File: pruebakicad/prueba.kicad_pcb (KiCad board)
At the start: 2 copper layers, 33 parts, among them J1 Conn_01x08_RC522, J2 Conn_01x04_MountingPin, J3 Conn_01x03, J4 Conn_2Rows-15Pins, J5 Conn_01x04, Q1 BSS138, Q2 BSS138, U1 TLV1117-33, U2 TLV1117-50, U3 ESP32-WROOM-32

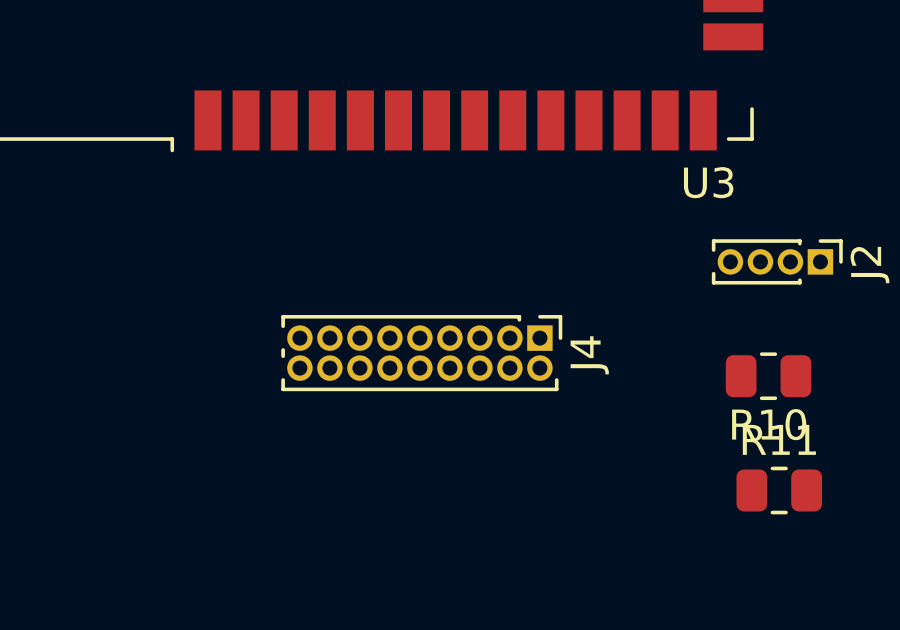
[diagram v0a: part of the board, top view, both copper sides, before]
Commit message: wires updated
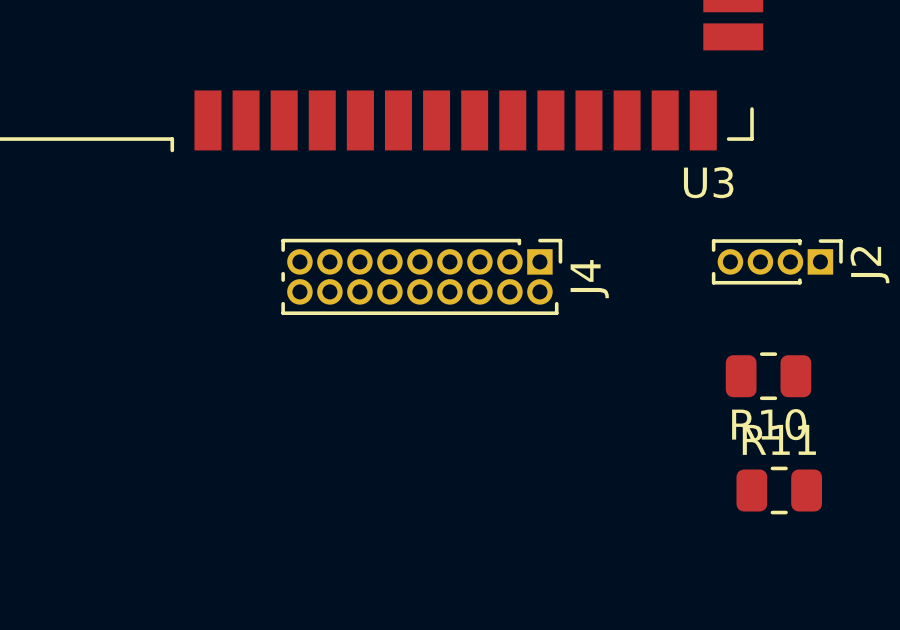
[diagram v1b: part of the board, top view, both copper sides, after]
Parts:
- moved J4 2.54 mm to (53.3, 114.3)
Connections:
- J4 pad 12: /sensVP -> Net-(J4-Pad12)
- J4 pad 13: /IO26 -> /sensVN
- J4 pad 14: /sensVN -> /sensVP
- J4 pad 15: GND -> +3V3
- J4 pad 16: +5V -> GND

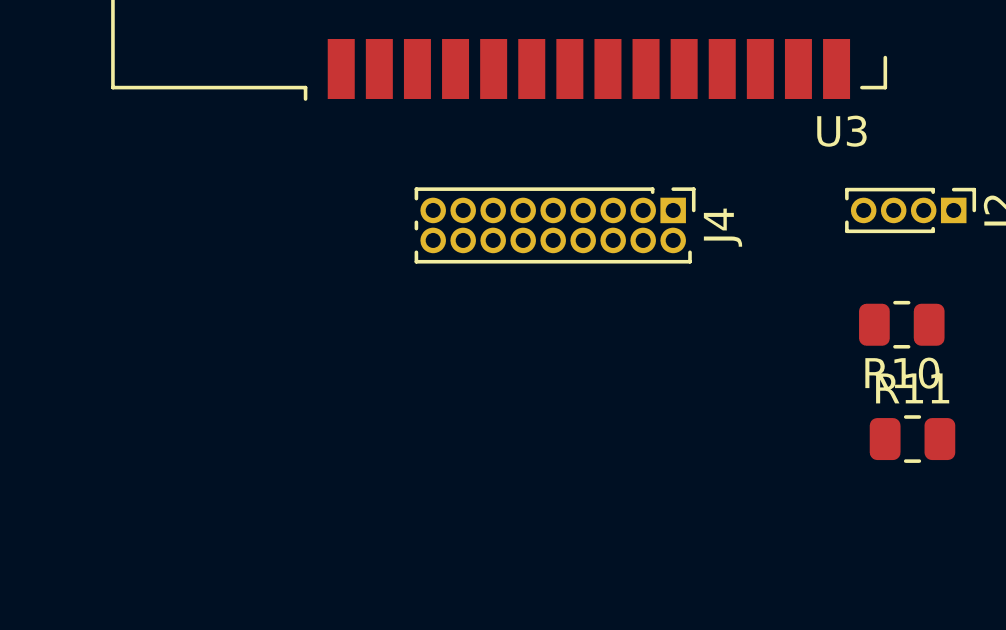
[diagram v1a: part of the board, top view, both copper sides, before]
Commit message: wires updated
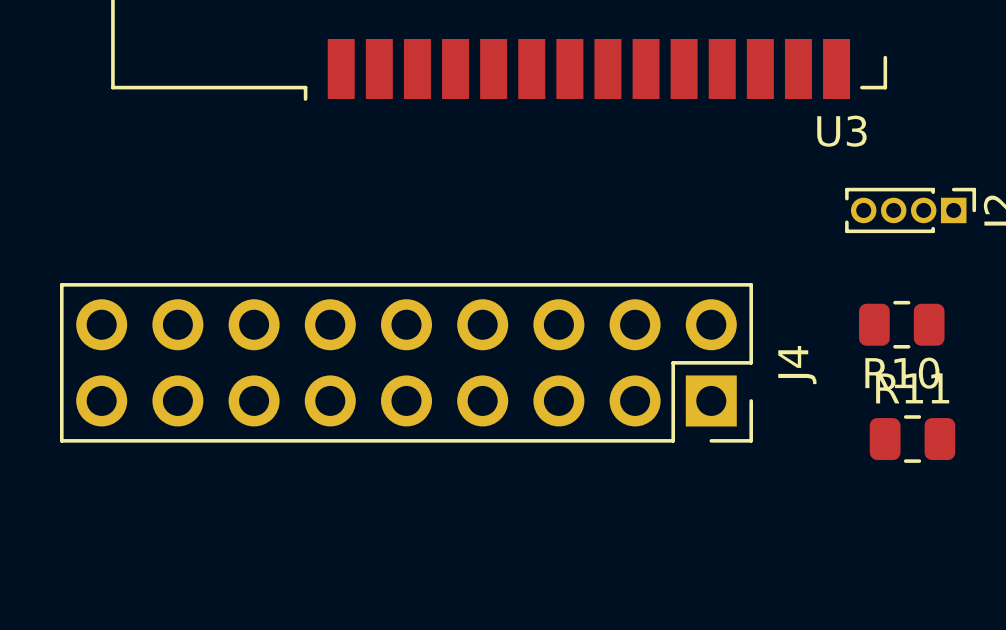
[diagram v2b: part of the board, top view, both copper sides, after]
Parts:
- J4: footprint Connector_PinHeader_1.00mm:PinHeader_2x09_P1.00mm_Vertical -> Connector_PinSocket_2.54mm:PinSocket_2x09_P2.54mm_Vertical
- moved J4 6.48 mm to (54.6, 120.7)
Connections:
- J4 pad 10: /IO35 -> /IO32
- J4 pad 11: /IO25 -> /IO35
- J4 pad 12: Net-(J4-Pad12) -> /IO34
- J4 pad 2: /IO27 -> Net-(J4-Pad2)
- J4 pad 3: /IO13 -> Net-(J4-Pad3)
- J4 pad 4: /IO32 -> Net-(J4-Pad4)
- J4 pad 5: /IO15 -> Net-(J4-Pad5)
- J4 pad 6: /IO33 -> /IO27
- J4 pad 7: /IO16 -> /IO26
- J4 pad 8: /IO34 -> /IO25
- J4 pad 9: /IO17 -> /IO33
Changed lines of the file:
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@@
     (zones 0)
     (modules 33)
-    (nets 49)
+    (nets 52)
   )
   (page A4)
@@
   (net 46 /esp32-wroom/IO0)
   (net 47 "Net-(U3-Pad32)")
-  (net 48 "Net-(J4-Pad12)")
+  (net 48 "Net-(J4-Pad4)")
+  (net 49 "Net-(J4-Pad2)")
+  (net 50 "Net-(J4-Pad5)")
+  (net 51 "Net-(J4-Pad3)")
   (net_class Default "This is the default net class."
     (clearance 0.2)
@@
     (add_net "Net-(C5-Pad1)")
     (add_net "Net-(J1-Pad5)")
-    (add_net "Net-(J4-Pad12)")
+    (add_net "Net-(J4-Pad2)")
+    (add_net "Net-(J4-Pad3)")
+    (add_net "Net-(J4-Pad4)")
+    (add_net "Net-(J4-Pad5)")
     (add_net "Net-(LedRed1-Pad2)")
     (add_net "Net-(Q1-Pad1)")
@@
     (add_net "Net-(U3-Pad22)")
     (add_net "Net-(U3-Pad32)")
+  )
+  (module Connector_PinSocket_2.54mm:PinSocket_2x09_P2.54mm_Vertical (layer F.Cu)
+    (at 54.61 120.65 270)
+    (descr "Through hole straight socket strip, 2x09, 2.54mm pitch, double cols (from Kicad 4.0.7), script generated")
+    (tags "Through hole socket strip THT 2x09 2.54mm double row")
+    (fp_text reference J4 (at -1.27 -2.77 90) (layer F.SilkS)
+      (effects (font (size 1 1) (thickness 0.15)))
+    )
+    (fp_text value Conn_2Rows-15Pins (at -1.27 23.09 90) (layer F.Fab)
+      (effects (font (size 1 1) (thickness 0.15)))
+    )
+    (fp_text user %R (at -1.27 10.16) (layer F.Fab)
+      (effects (font (size 1 1) (thickness 0.15)))
+    )
+    (fp_line (start -3.81 -1.27) (end 0.27 -1.27) (layer F.Fab) (width 0.1))
+    (fp_line (start 0.27 -1.27) (end 1.27 -0.27) (layer F.Fab) (width 0.1))
+    (fp_line (start 1.27 -0.27) (end 1.27 21.59) (layer F.Fab) (width 0.1))
+    (fp_line (start 1.27 21.59) (end -3.81 21.59) (layer F.Fab) (width 0.1))
+    (fp_line (start -3.81 21.59) (end -3.81 -1.27) (layer F.Fab) (width 0.1))
+    (fp_line (start -3.87 -1.33) (end -1.27 -1.33) (layer F.SilkS) (width 0.12))
+    (fp_line (start -3.87 -1.33) (end -3.87 21.65) (layer F.SilkS) (width 0.12))
+    (fp_line (start -3.87 21.65) (end 1.33 21.65) (layer F.SilkS) (width 0.12))
+    (fp_line (start 1.33 1.27) (end 1.33 21.65) (layer F.SilkS) (width 0.12))
+    (fp_line (start -1.27 1.27) (end 1.33 1.27) (layer F.SilkS) (width 0.12))
+    (fp_line (start -1.27 -1.33) (end -1.27 1.27) (layer F.SilkS) (width 0.12))
+    (fp_line (start 1.33 -1.33) (end 1.33 0) (layer F.SilkS) (width 0.12))
+    (fp_line (start 0 -1.33) (end 1.33 -1.33) (layer F.SilkS) (width 0.12))
+    (fp_line (start -4.34 -1.8) (end 1.76 -1.8) (layer F.CrtYd) (width 0.05))
+    (fp_line (start 1.76 -1.8) (end 1.76 22.1) (layer F.CrtYd) (width 0.05))
+    (fp_line (start 1.76 22.1) (end -4.34 22.1) (layer F.CrtYd) (width 0.05))
+    (fp_line (start -4.34 22.1) (end -4.34 -1.8) (layer F.CrtYd) (width 0.05))
+    (pad 18 thru_hole oval (at -2.54 20.32 270) (size 1.7 1.7) (drill 1) (layers *.Cu *.Mask))
+    (pad 17 thru_hole oval (at 0 20.32 270) (size 1.7 1.7) (drill 1) (layers *.Cu *.Mask)
+      (net 4 GND))
+    (pad 16 thru_hole oval (at -2.54 17.78 270) (size 1.7 1.7) (drill 1) (layers *.Cu *.Mask)
+      (net 4 GND))
+    (pad 15 thru_hole oval (at 0 17.78 270) (size 1.7 1.7) (drill 1) (layers *.Cu *.Mask)
+      (net 5 +3V3))
+    (pad 14 thru_hole oval (at -2.54 15.24 270) (size 1.7 1.7) (drill 1) (layers *.Cu *.Mask)
+      (net 29 /sensVP))
+    (pad 13 thru_hole oval (at 0 15.24 270) (size 1.7 1.7) (drill 1) (layers *.Cu *.Mask)
+      (net 31 /sensVN))
+    (pad 12 thru_hole oval (at -2.54 12.7 270) (size 1.7 1.7) (drill 1) (layers *.Cu *.Mask)
+      (net 25 /IO34))
+    (pad 11 thru_hole oval (at 0 12.7 270) (size 1.7 1.7) (drill 1) (layers *.Cu *.Mask)
+      (net 27 /IO35))
+    (pad 10 thru_hole oval (at -2.54 10.16 270) (size 1.7 1.7) (drill 1) (layers *.Cu *.Mask)
+      (net 21 /IO32))
+    (pad 9 thru_hole oval (at 0 10.16 270) (size 1.7 1.7) (drill 1) (layers *.Cu *.Mask)
+      (net 23 /IO33))
+    (pad 8 thru_hole oval (at -2.54 7.62 270) (size 1.7 1.7) (drill 1) (layers *.Cu *.Mask)
+      (net 28 /IO25))
+    (pad 7 thru_hole oval (at 0 7.62 270) (size 1.7 1.7) (drill 1) (layers *.Cu *.Mask)
+      (net 30 /IO26))
+    (pad 6 thru_hole oval (at -2.54 5.08 270) (size 1.7 1.7) (drill 1) (layers *.Cu *.Mask)
+      (net 20 /IO27))
+    (pad 5 thru_hole oval (at 0 5.08 270) (size 1.7 1.7) (drill 1) (layers *.Cu *.Mask)
+      (net 50 "Net-(J4-Pad5)"))
+    (pad 4 thru_hole oval (at -2.54 2.54 270) (size 1.7 1.7) (drill 1) (layers *.Cu *.Mask)
+      (net 48 "Net-(J4-Pad4)"))
+    (pad 3 thru_hole oval (at 0 2.54 270) (size 1.7 1.7) (drill 1) (layers *.Cu *.Mask)
+      (net 51 "Net-(J4-Pad3)"))
+    (pad 2 thru_hole oval (at -2.54 0 270) (size 1.7 1.7) (drill 1) (layers *.Cu *.Mask)
+      (net 49 "Net-(J4-Pad2)"))
+    (pad 1 thru_hole rect (at 0 0 270) (size 1.7 1.7) (drill 1) (layers *.Cu *.Mask)
+      (net 5 +3V3))
+    (model ${KISYS3DMOD}/Connector_PinSocket_2.54mm.3dshapes/PinSocket_2x09_P2.54mm_Vertical.wrl
+      (at (xyz 0 0 0))
+      (scale (xyz 1 1 1))
+      (rotate (xyz 0 0 0))
+    )
   )
   (module LED_SMD:LED_0805_2012Metric (layer F.Cu)
@@
       (at (xyz 0 0 0))
       (scale (xyz 1 1 1))
-      (rotate (xyz 0 0 0))
-    )
-  )
-  (module Connector_PinHeader_1.00mm:PinHeader_2x09_P1.00mm_Vertical (layer F.Cu)
-    (at 53.34 114.3 270)
-    (descr "Through hole straight pin header, 2x09, 1.00mm pitch, double rows")
-    (tags "Through hole pin header THT 2x09 1.00mm double row")
-    (fp_text reference J4 (at 0.5 -1.56 90) (layer F.SilkS)
-      (effects (font (size 1 1) (thickness 0.15)))
-    )
-    (fp_text value Conn_2Rows-15Pins (at 0.5 9.56 90) (layer F.Fab)
-      (effects (font (size 1 1) (thickness 0.15)))
-    )
-    (fp_line (start -0.075 -0.5) (end 1.65 -0.5) (layer F.Fab) (width 0.1))
-    (fp_line (start 1.65 -0.5) (end 1.65 8.5) (layer F.Fab) (width 0.1))
-    (fp_line (start 1.65 8.5) (end -0.65 8.5) (layer F.Fab) (width 0.1))
-    (fp_line (start -0.65 8.5) (end -0.65 0.075) (layer F.Fab) (width 0.1))
-    (fp_line (start -0.65 0.075) (end -0.075 -0.5) (layer F.Fab) (width 0.1))
-    (fp_line (start -0.71 8.56) (end -0.394493 8.56) (layer F.SilkS) (width 0.12))
-    (fp_line (start 1.394493 8.56) (end 1.71 8.56) (layer F.SilkS) (width 0.12))
-    (fp_line (start 0.394493 8.56) (end 0.605507 8.56) (layer F.SilkS) (width 0.12))
-    (fp_line (start -0.71 0.685) (end -0.71 8.56) (layer F.SilkS) (width 0.12))
-    (fp_line (start 1.71 -0.56) (end 1.71 8.56) (layer F.SilkS) (width 0.12))
-    (fp_line (start -0.71 0.685) (end -0.608276 0.685) (layer F.SilkS) (width 0.12))
-    (fp_line (start 1.394493 -0.56) (end 1.71 -0.56) (layer F.SilkS) (width 0.12))
-    (fp_line (start -0.71 0) (end -0.71 -0.685) (layer F.SilkS) (width 0.12))
-    (fp_line (start -0.71 -0.685) (end 0 -0.685) (layer F.SilkS) (width 0.12))
-    (fp_line (start -1.15 -1) (end -1.15 9) (layer F.CrtYd) (width 0.05))
-    (fp_line (start -1.15 9) (end 2.15 9) (layer F.CrtYd) (width 0.05))
-    (fp_line (start 2.15 9) (end 2.15 -1) (layer F.CrtYd) (width 0.05))
-    (fp_line (start 2.15 -1) (end -1.15 -1) (layer F.CrtYd) (width 0.05))
-    (fp_text user %R (at 0.5 4) (layer F.Fab)
-      (effects (font (size 1 1) (thickness 0.15)))
-    )
-    (pad 1 thru_hole rect (at 0 0 270) (size 0.85 0.85) (drill 0.5) (layers *.Cu *.Mask)
-      (net 5 +3V3))
-    (pad 2 thru_hole oval (at 1 0 270) (size 0.85 0.85) (drill 0.5) (layers *.Cu *.Mask)
-      (net 20 /IO27))
-    (pad 3 thru_hole oval (at 0 1 270) (size 0.85 0.85) (drill 0.5) (layers *.Cu *.Mask)
-      (net 2 /IO13))
-    (pad 4 thru_hole oval (at 1 1 270) (size 0.85 0.85) (drill 0.5) (layers *.Cu *.Mask)
-      (net 21 /IO32))
-    (pad 5 thru_hole oval (at 0 2 270) (size 0.85 0.85) (drill 0.5) (layers *.Cu *.Mask)
-      (net 22 /IO15))
-    (pad 6 thru_hole oval (at 1 2 270) (size 0.85 0.85) (drill 0.5) (layers *.Cu *.Mask)
-      (net 23 /IO33))
-    (pad 7 thru_hole oval (at 0 3 270) (size 0.85 0.85) (drill 0.5) (layers *.Cu *.Mask)
-      (net 24 /IO16))
-    (pad 8 thru_hole oval (at 1 3 270) (size 0.85 0.85) (drill 0.5) (layers *.Cu *.Mask)
-      (net 25 /IO34))
-    (pad 9 thru_hole oval (at 0 4 270) (size 0.85 0.85) (drill 0.5) (layers *.Cu *.Mask)
-      (net 26 /IO17))
-    (pad 10 thru_hole oval (at 1 4 270) (size 0.85 0.85) (drill 0.5) (layers *.Cu *.Mask)
-      (net 27 /IO35))
-    (pad 11 thru_hole oval (at 0 5 270) (size 0.85 0.85) (drill 0.5) (layers *.Cu *.Mask)
-      (net 28 /IO25))
-    (pad 12 thru_hole oval (at 1 5 270) (size 0.85 0.85) (drill 0.5) (layers *.Cu *.Mask)
-      (net 48 "Net-(J4-Pad12)"))
-    (pad 13 thru_hole oval (at 0 6 270) (size 0.85 0.85) (drill 0.5) (layers *.Cu *.Mask)
-      (net 31 /sensVN))
-    (pad 14 thru_hole oval (at 1 6 270) (size 0.85 0.85) (drill 0.5) (layers *.Cu *.Mask)
-      (net 29 /sensVP))
-    (pad 15 thru_hole oval (at 0 7 270) (size 0.85 0.85) (drill 0.5) (layers *.Cu *.Mask)
-      (net 5 +3V3))
-    (pad 16 thru_hole oval (at 1 7 270) (size 0.85 0.85) (drill 0.5) (layers *.Cu *.Mask)
-      (net 4 GND))
-    (pad 17 thru_hole oval (at 0 8 270) (size 0.85 0.85) (drill 0.5) (layers *.Cu *.Mask)
-      (net 4 GND))
-    (pad 18 thru_hole oval (at 1 8 270) (size 0.85 0.85) (drill 0.5) (layers *.Cu *.Mask))
-    (model ${KISYS3DMOD}/Connector_PinHeader_1.00mm.3dshapes/PinHeader_2x09_P1.00mm_Vertical.wrl
-      (at (xyz 0 0 0))
-      (scale (xyz 1 1 1))

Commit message: wires
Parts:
- J1: footprint Connector_PinHeader_1.00mm:PinHeader_1x08_P1.00mm_Vertical -> Connector_PinSocket_2.54mm:PinSocket_1x08_P2.54mm_Vertical
- J2, J5: footprint Connector_PinHeader_1.00mm:PinHeader_1x04_P1.00mm_Vertical -> Connector_PinSocket_2.54mm:PinSocket_1x04_P2.54mm_Vertical
- J4: footprint Connector_PinSocket_2.54mm:PinSocket_2x09_P2.54mm_Vertical -> Connector_PinSocket_2.54mm:PinSocket_2x07_P2.54mm_Vertical
- moved J1 81.6 mm to (24.1, 110.5), turned to 180 degrees
- moved J3 14.0 mm to (106.7, 92.7)
- moved BZ1 14.0 mm to (94.0, 99.1)
- moved Blue1 14.0 mm to (92.7, 87.6)
- moved C2 14.0 mm to (81.3, 110.5)
- moved C6 14.0 mm to (111.8, 88.9)
- moved Cin1 14.0 mm to (107.4, 105.4)
- moved Cin2 14.0 mm to (107.4, 113.0)
- moved Cout1 14.0 mm to (109.2, 121.9)
- moved Cout2 14.0 mm to (85.3, 121.9)
- moved LedRed1 14.0 mm to (100.3, 87.6)
- moved Q1 14.0 mm to (87.6, 96.5)
- moved Q2 14.0 mm to (87.6, 101.6)
- moved R1 14.0 mm to (81.6, 114.3)
- moved R3 14.0 mm to (87.6, 105.4)
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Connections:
- J4 pad 1: +3V3 -> +5V
- J4 pad 10: /IO32 -> /sensVN
- J4 pad 11: /IO35 -> +3V3
- J4 pad 12: /IO34 -> +3V3
- J4 pad 13: /sensVN -> GND
- J4 pad 14: /sensVP -> GND
- J4 pad 2: Net-(J4-Pad2) -> /IO27
- J4 pad 3: Net-(J4-Pad3) -> /IO25
- J4 pad 4: Net-(J4-Pad4) -> /IO26
- J4 pad 5: Net-(J4-Pad5) -> /IO32
- J4 pad 6: /IO27 -> /IO33
- J4 pad 7: /IO26 -> /IO34
- J4 pad 8: /IO25 -> /IO35
- J4 pad 9: /IO33 -> /sensVP
